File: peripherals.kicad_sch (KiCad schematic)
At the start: 16 parts, among them J10 0533980471, J7 522711069, J8 522711069, U33 NTS0102, U9 NTS0102

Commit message: Initial layout attempt
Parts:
- removed J8: 522711069, JetsonCarrier:CON_522711069_MOL, symbol Connector_Generic_MountingPin:Conn_01x10_MountingPin
- added H10, H9: MountingHole_Pad, MountingHole:MountingHole_2.5mm_Pad_Via, symbol Mechanical:MountingHole_Pad
- added J12: QTH-030-01-L-D-A, Argus-Connectors:SAMTEC-QTH-030-01-X-D-A, symbol Connector_Generic_Shielded:Conn_02x30_Odd_Even_Shielded
- added J9: QSH-030-01-L-D-A, Argus-Connectors:SAMTEC_QSH-030-01-L-D-A, symbol Connector_Generic_Shielded:Conn_02x30_Odd_Even_Shielded
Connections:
- net GND: now also H10.1, H9.1, J12.11 (Pin_11), J12.12 (Pin_12), J12.13 (Pin_13), J12.14 (Pin_14), J12.15 (Pin_15), J12.16 (Pin_16), J12.17 (Pin_17), J12.18 (Pin_18), J12.19 (Pin_19), J12.20 (Pin_20), J12.25 (Pin_25), J12.26 (Pin_26), J12.27 (Pin_27), J12.28 (Pin_28), J12.35 (Pin_35), J12.41 (Pin_41), J12.44 (Pin_44), J12.47 (Pin_47), J12.59 (Pin_59), J12.60 (Pin_60), J12.SH (Shield), J9.11 (Pin_11), J9.12 (Pin_12), J9.13 (Pin_13), J9.14 (Pin_14), J9.15 (Pin_15), J9.16 (Pin_16), J9.17 (Pin_17), J9.18 (Pin_18), J9.19 (Pin_19), J9.20 (Pin_20), J9.25 (Pin_25), J9.26 (Pin_26), J9.27 (Pin_27), J9.28 (Pin_28), J9.35 (Pin_35), J9.41 (Pin_41), J9.44 (Pin_44), J9.47 (Pin_47), J9.59 (Pin_59), J9.60 (Pin_60), J9.SH (Shield)
- new net +3V3_BUS: J12.21 (Pin_21), J12.22 (Pin_22), J12.23 (Pin_23), J12.24 (Pin_24), J9.21 (Pin_21), J9.22 (Pin_22), J9.23 (Pin_23), J9.24 (Pin_24)
- new net Pin_29: J12.29 (Pin_29), J9.29 (Pin_29)
- new net Pin_30: J12.30 (Pin_30), J9.30 (Pin_30)
- new net Pin_31: J12.31 (Pin_31), J9.31 (Pin_31)
- new net Pin_32: J12.32 (Pin_32), J9.32 (Pin_32)
- new net Pin_33: J12.33 (Pin_33), J9.33 (Pin_33)
- new net Pin_34: J12.34 (Pin_34), J9.34 (Pin_34)
- new net Pin_36: J12.36 (Pin_36), J9.36 (Pin_36)
- new net Pin_38: J12.38 (Pin_38), J9.38 (Pin_38)
- new net Pin_40: J12.40 (Pin_40), J9.40 (Pin_40)
- new net Pin_42: J12.42 (Pin_42), J9.42 (Pin_42)
- new net Pin_43: J12.43 (Pin_43), J9.43 (Pin_43)
- new net Pin_45: J12.45 (Pin_45), J9.45 (Pin_45)
- new net Pin_46: J12.46 (Pin_46), J9.46 (Pin_46)
- new net Pin_48: J12.48 (Pin_48), J9.48 (Pin_48)
- new net Pin_49: J12.49 (Pin_49), J9.49 (Pin_49)
- new net Pin_50: J12.50 (Pin_50), J9.50 (Pin_50)
- new net Pin_51: J12.51 (Pin_51), J9.51 (Pin_51)
- new net Pin_52: J12.52 (Pin_52), J9.52 (Pin_52)
- new net Pin_53: J12.53 (Pin_53), J9.53 (Pin_53)
- new net Pin_54: J12.54 (Pin_54), J9.54 (Pin_54)
- new net Pin_55: J12.55 (Pin_55), J9.55 (Pin_55)
- new net Pin_56: J12.56 (Pin_56), J9.56 (Pin_56)
- new net Pin_57: J12.57 (Pin_57), J9.57 (Pin_57)
- new net Pin_58: J12.58 (Pin_58), J9.58 (Pin_58)
- new net SCL: J12.37 (Pin_37), J9.37 (Pin_37)
- new net SDA: J12.39 (Pin_39), J9.39 (Pin_39)
- new net VBATT: J12.1 (Pin_1), J12.10 (Pin_10), J12.2 (Pin_2), J12.3 (Pin_3), J12.4 (Pin_4), J12.5 (Pin_5), J12.6 (Pin_6), J12.7 (Pin_7), J12.8 (Pin_8), J12.9 (Pin_9), J9.1 (Pin_1), J9.10 (Pin_10), J9.2 (Pin_2), J9.3 (Pin_3), J9.4 (Pin_4), J9.5 (Pin_5), J9.6 (Pin_6), J9.7 (Pin_7), J9.8 (Pin_8), J9.9 (Pin_9)

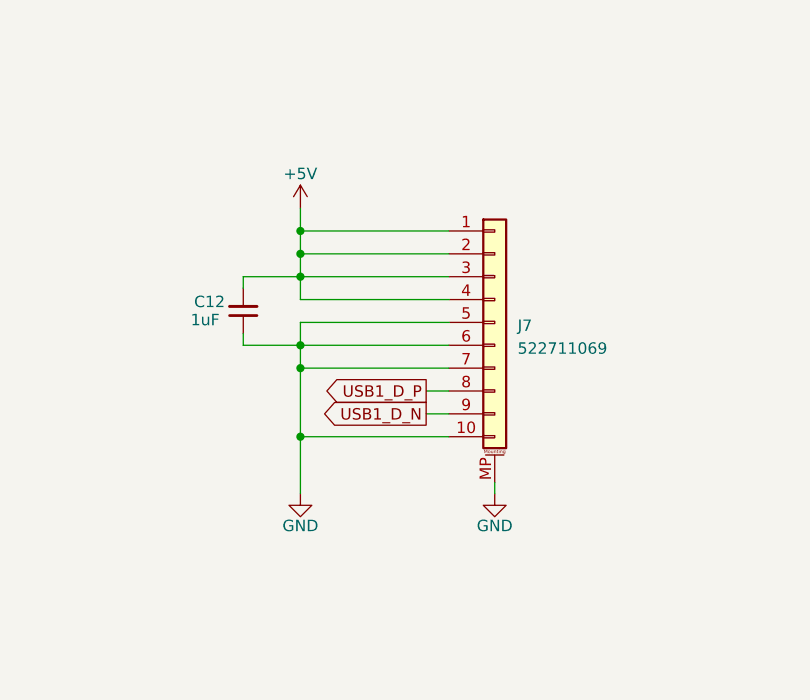
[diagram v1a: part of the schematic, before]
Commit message: Finish HDMI routing, replace usbc w/ usba
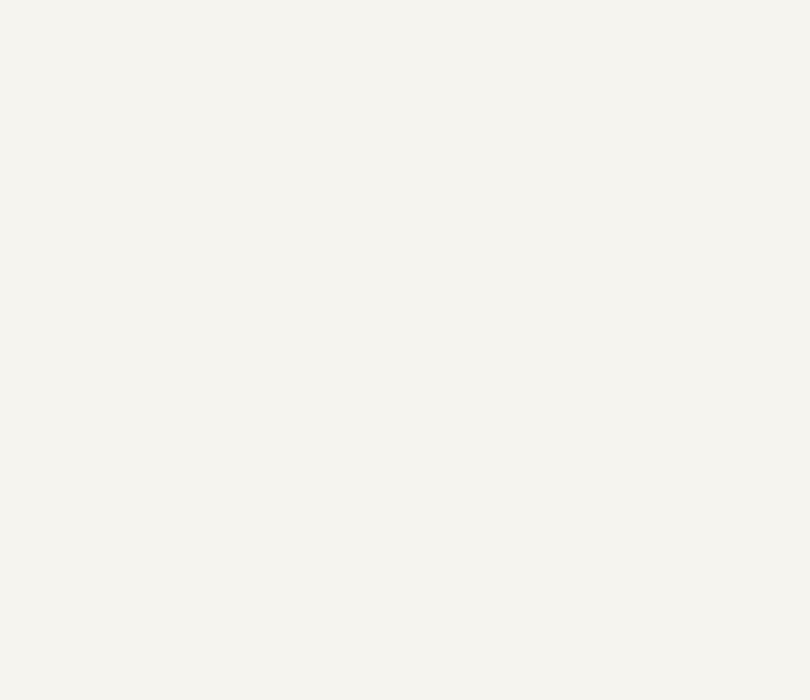
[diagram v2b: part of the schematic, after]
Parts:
- removed C12: 1uF, Capacitor_SMD:C_0603_1608Metric, symbol Device:C_Small
- removed J7: 522711069, JetsonCarrier:CON_522711069_MOL, symbol Connector_Generic_MountingPin:Conn_01x10_MountingPin

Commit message: Power routing, CSI length matching, cleanup
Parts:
- added C53, C54, C55: 100nF, Capacitor_SMD:C_0603_1608Metric, symbol Device:C_Small
- added R108: 0R, Resistor_SMD:R_0402_1005Metric, symbol Device:R_Small
- added R20: 120R, Resistor_SMD:R_0402_1005Metric, symbol Device:R_Small
- added TP32, TP33: TP_0.75mm_SMD, JetsonCarrier:TP_SMD_0.75mm, symbol Connector:TestPoint
- added U10: NTS0102, Argus-IC:NXP_XSON-8, symbol JetsonCarrier:NTS0102
- added U2: MAX3051, Package_TO_SOT_SMD:SOT-23-8, symbol Interface_UART:MAX3051
- U33, U9: footprint JetsonCarrier:XSON-8_1x1.95mm_P0.5mm -> Argus-IC:NXP_XSON-8
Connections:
- net Pin_29 is gone; now on net MB_SPI_SCK: J12.29 (Pin_29), J9.29 (Pin_29)
- net Pin_31 is gone; now on net MB_SPI_MOSI: J12.31 (Pin_31), J9.31 (Pin_31)
- net Pin_46 is gone; now on net SYS_ENABLE: J12.46 (Pin_46), J9.46 (Pin_46)
- net SCL is gone; now on net MB_SCL: J12.37 (Pin_37), J9.37 (Pin_37)
- net SDA is gone; now on net MB_SDA: J12.39 (Pin_39), J9.39 (Pin_39)
- net +1V8: now also C53.1, U10.3 (VCC_{A}), U10.6 (OE)
- net +3V3: now also C54.1, C55.1, U10.7 (VCC_{B}), U2.3 (VDD)
- net GND: now also C53.2, C54.2, C55.2, R108.2, U10.2 (GND), U2.2 (GND)
- net MB_JETSON_RX renamed MB_SPI_MOSI
- net MB_JETSON_TX renamed MB_SPI_SCK
- net Pin_33 renamed MB_SPI_MISO
- net MB_SPI_MISO: now also U10.1 (B_{2})
- net Pin_48 renamed MB_JETSON_CS
- net MB_JETSON_CS: now also U10.8 (B_{1})
- net UART1_RXD renamed SPI0_MOSI
- net UART1_TXD renamed SPI0_SCK
- new net: R20.1, TP32.1, U2.7 (CANH)
- new net: R20.2, TP33.1, U2.6 (CANL)
- new net: R108.1, U2.8 (RS)
- new net CAN_RXD: U2.4 (RXD)
- new net CAN_TXD: U2.1 (TXD)
- new net SPI0_MISO: U10.4 (A_{2})
- new net ~{SPI0_CS}: U10.5 (A_{1})
- no-connect marks 0 -> 1
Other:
- note removed: "USB 2.0 FPC Connector"
- moved on the sheet: C40, C41, C44, C48, D8, H10, H9, J10, J12, J9, R15, R18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

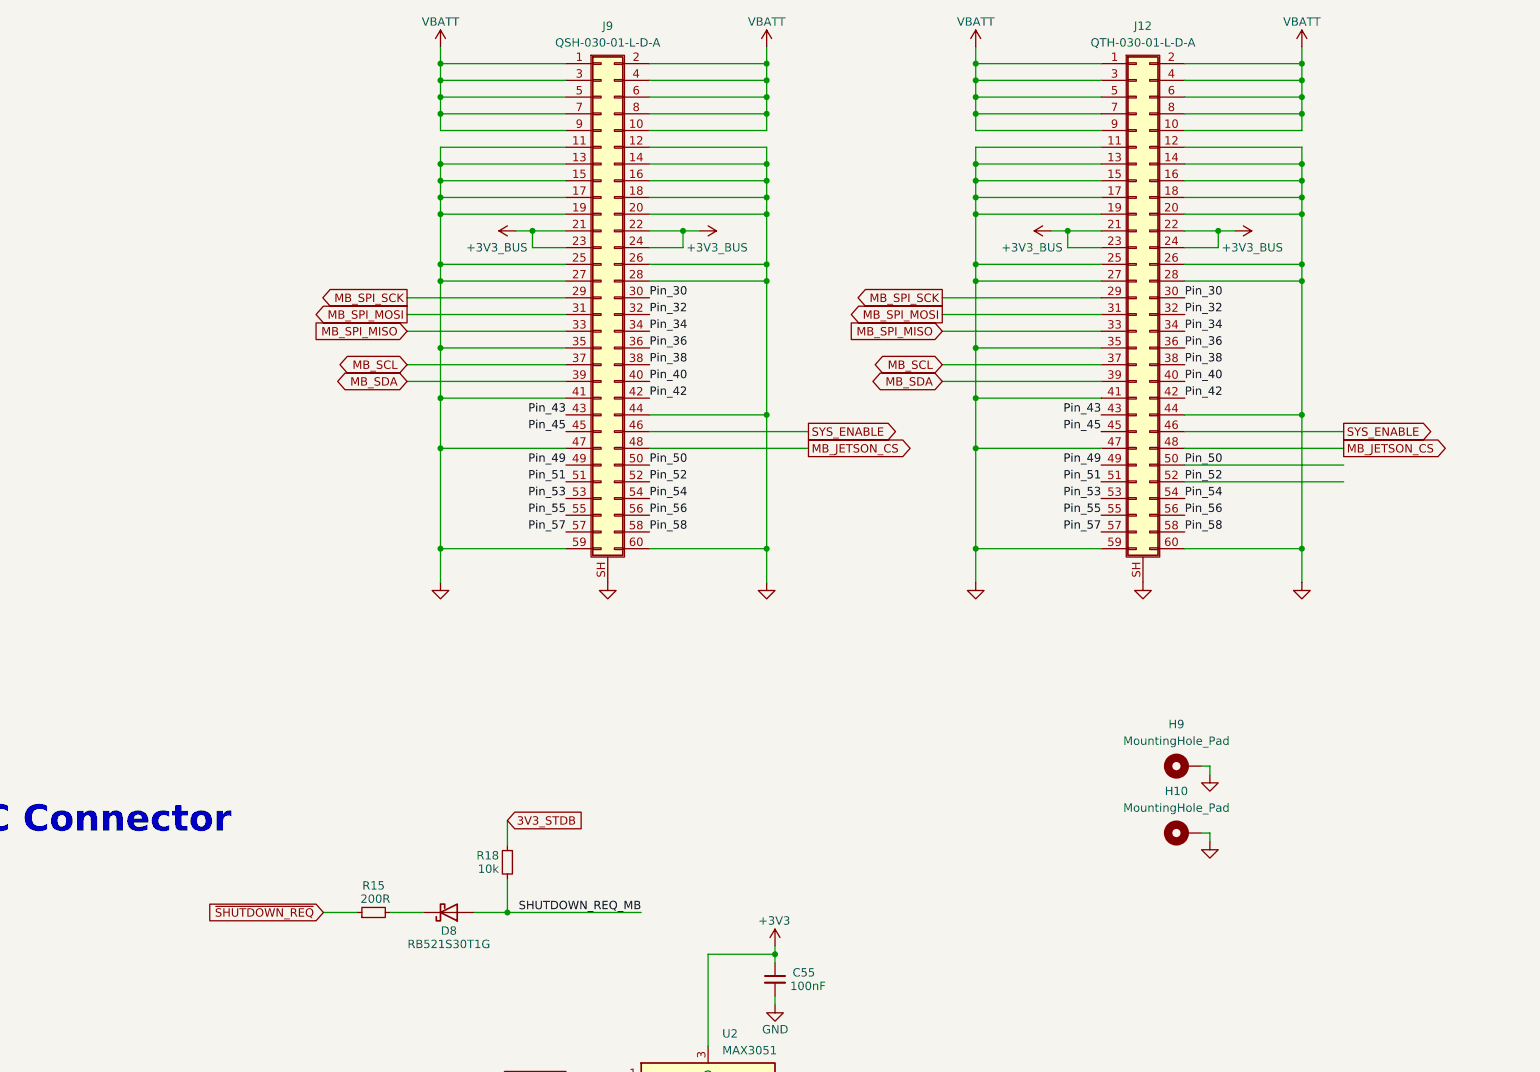
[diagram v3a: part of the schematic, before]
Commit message: Add power sequencing logic, layout
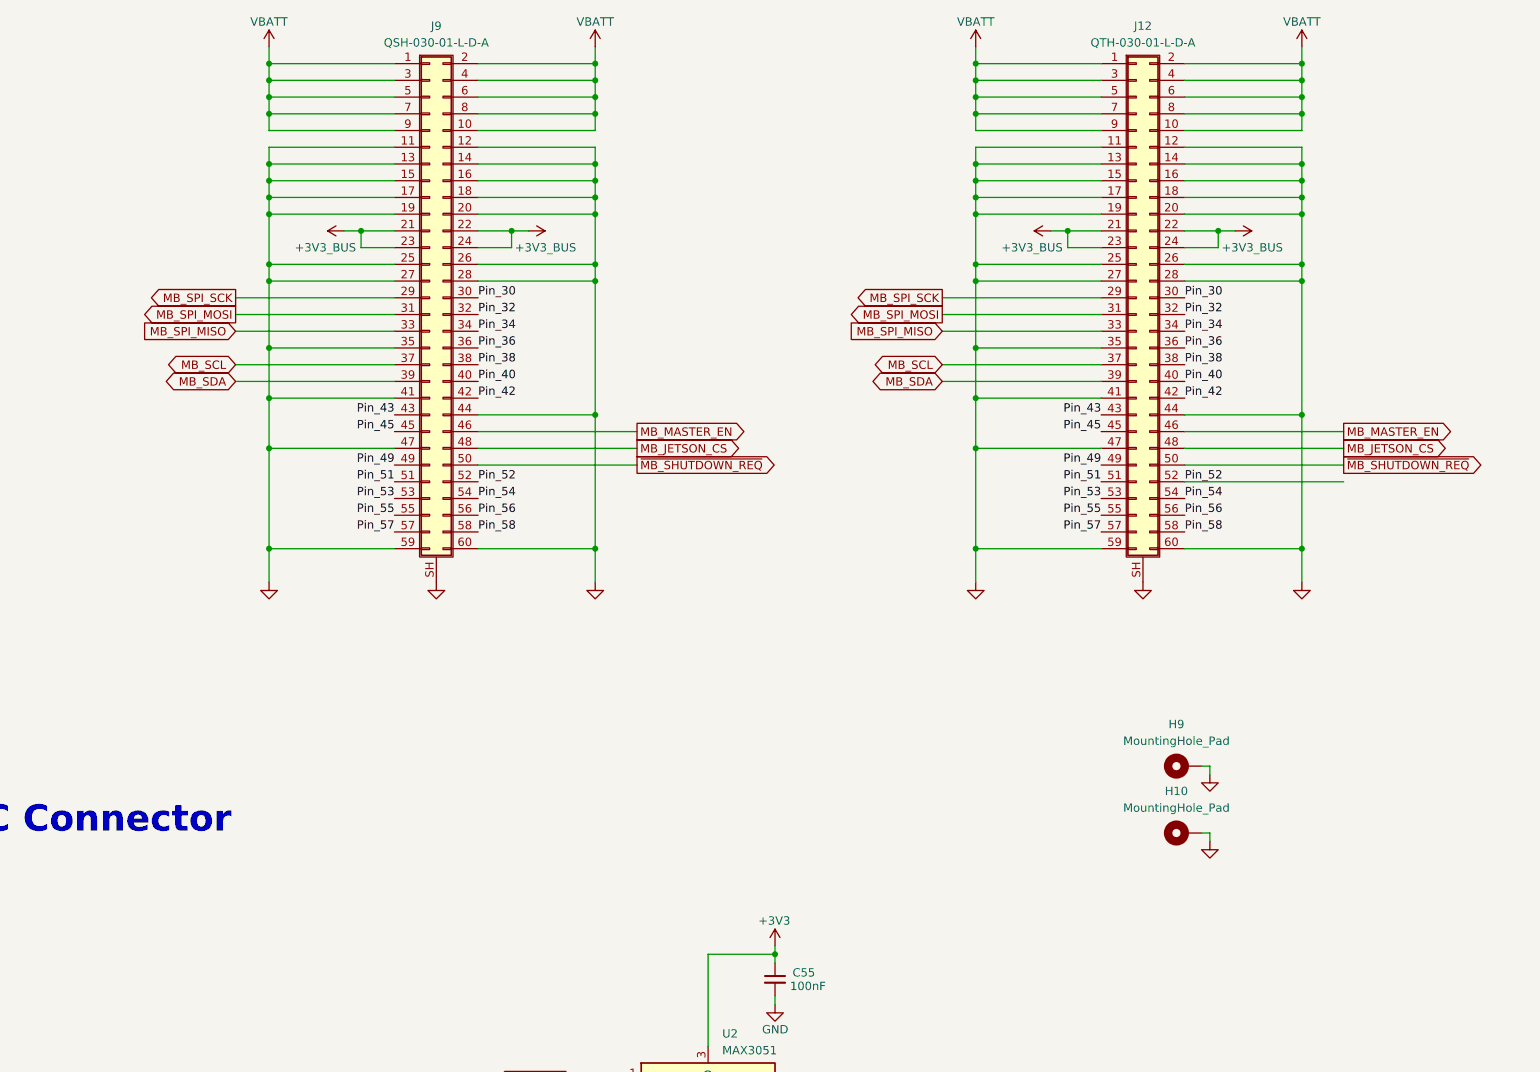
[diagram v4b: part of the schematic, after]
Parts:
- removed D8: RB521S30T1G, Diode_SMD:D_SOD-523, symbol Device:D_Schottky
- removed R15: 200R, Resistor_SMD:R_0402_1005Metric, symbol Device:R_Small
- removed R18: 10k, Resistor_SMD:R_0402_1005Metric, symbol Device:R_Small
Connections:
- net Pin_50 renamed ~{MB_SHUTDOWN_REQ}
- net SYS_ENABLE renamed MB_MASTER_EN
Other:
- moved on the sheet: J9

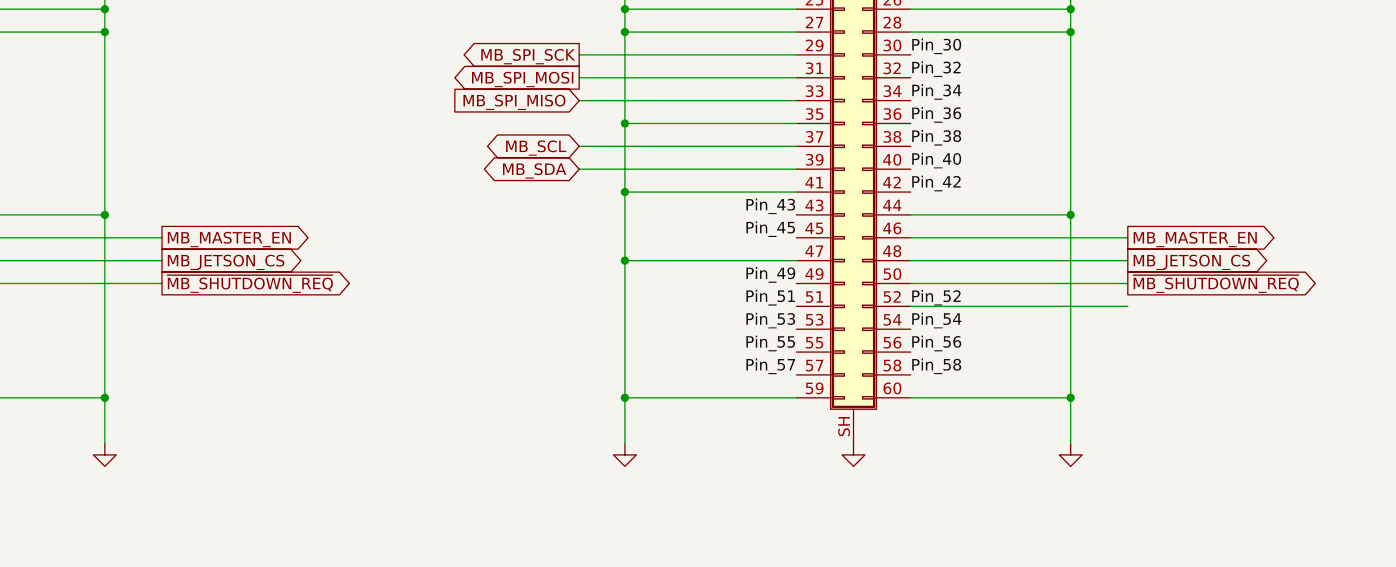
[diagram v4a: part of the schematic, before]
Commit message: Add bus protection, upgrade sequencer
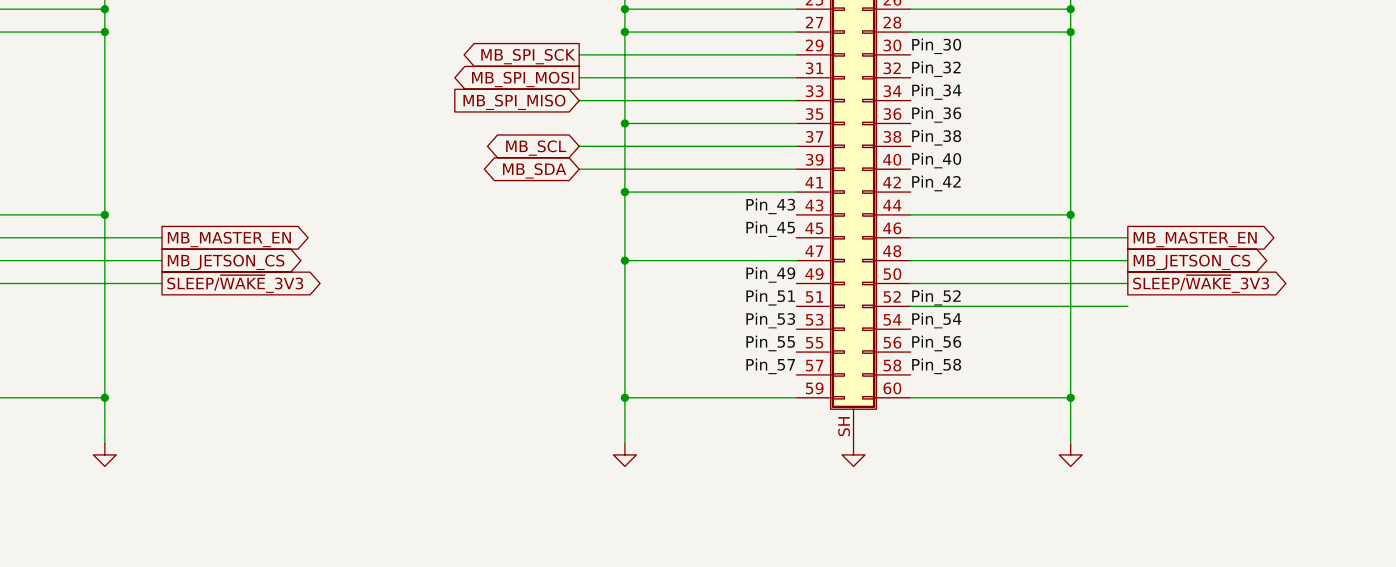
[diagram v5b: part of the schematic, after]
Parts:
- R108, R20: footprint Resistor_SMD:R_0402_1005Metric -> Resistor_SMD:R_0603_1608Metric
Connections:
- net ~{MB_SHUTDOWN_REQ} renamed SLEEP/~{WAKE}_3V3
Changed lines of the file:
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@@
-		)
-	)
-	(global_label "~{MB_SHUTDOWN_REQ}"
-		(shape output)
-		(at 221.615 139.7 0)
-		(fields_autoplaced yes)
-		(effects
-			(font
-				(size 1.27 1.27)
-			)
-			(justify left)
-		)
-		(property "Intersheetrefs" "${INTERSHEET_REFS}"
-			(at 243.2268 139.7 0)
-			(show_name no)
-			(do_not_autoplace no)
-			(effects
-				(font
-					(size 1.27 1.27)
-				)
-				(justify left)
-			)
 		)
 	)
@@
 		)
 	)
-	(global_label "~{MB_SHUTDOWN_REQ}"
+	(global_label "SLEEP{slash}~{WAKE}_3V3"
+		(shape output)
+		(at 221.615 139.7 0)
+		(effects
+			(font
+				(size 1.27 1.27)
+			)
+			(justify left)
+		)
+		(property "Intersheetrefs" "${INTERSHEET_REFS}"
+			(at 239.395 139.7 0)
+			(show_name no)
+			(do_not_autoplace no)
+			(effects
+				(font
+					(size 1.27 1.27)
+				)
+				(justify left)
+			)
+		)
+	)
+	(global_label "SLEEP{slash}~{WAKE}_3V3"
 		(shape output)
 		(at 328.93 139.7 0)
-		(fields_autoplaced yes)
 		(effects
 			(font
@@
 		)
 		(property "Intersheetrefs" "${INTERSHEET_REFS}"
-			(at 350.5418 139.7 0)
+			(at 346.71 139.7 0)
 			(show_name no)
 			(do_not_autoplace no)
@@
 			)
 		)
-		(property "Footprint" "Resistor_SMD:R_0402_1005Metric"
+		(property "Footprint" "Resistor_SMD:R_0603_1608Metric"
 			(at 255.905 238.125 0)
 			(hide yes)
@@
 			)
 		)
-		(property "Footprint" "Resistor_SMD:R_0402_1005Metric"
+		(property "Footprint" "Resistor_SMD:R_0603_1608Metric"
 			(at 213.36 243.205 0)
 			(hide yes)
